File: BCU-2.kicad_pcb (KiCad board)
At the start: 2 copper layers, 106 x 91.4 mm, 92 parts, among them J1 Screw_Terminal_01x04, J2 Conn_01x12_Male, J3 Screw_Terminal_01x04, J4 Conn_01x05_Male, J5 Conn_01x05_Male, J6 Conn_01x04_Male, J7 Conn_01x04_Male, Q1 2N7002, Q2 NTF6P02, Q3 2N7002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

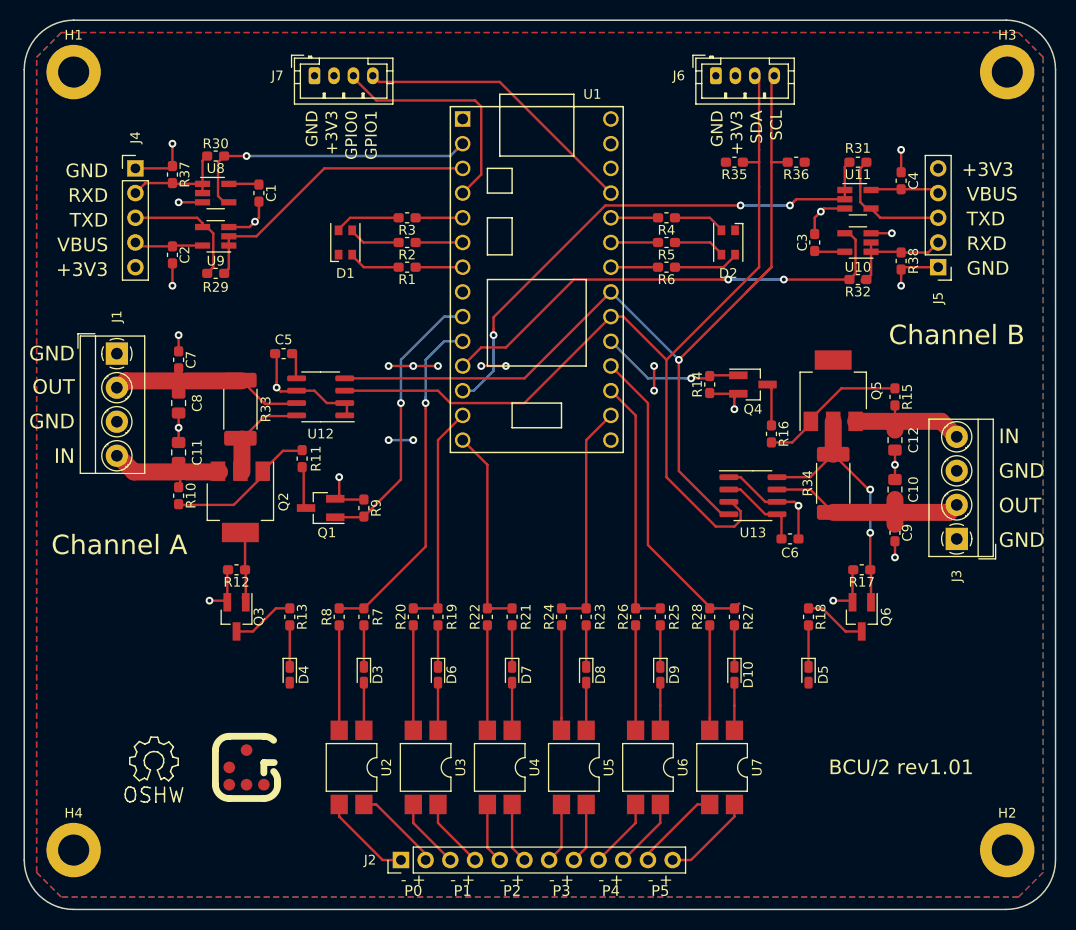
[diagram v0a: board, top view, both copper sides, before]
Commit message: PCB: Remove unneeded stubs to fix track has unconnected end warnings
Signed-off-by: Geert Uytterhoeven <geert@linux-m68k.org>
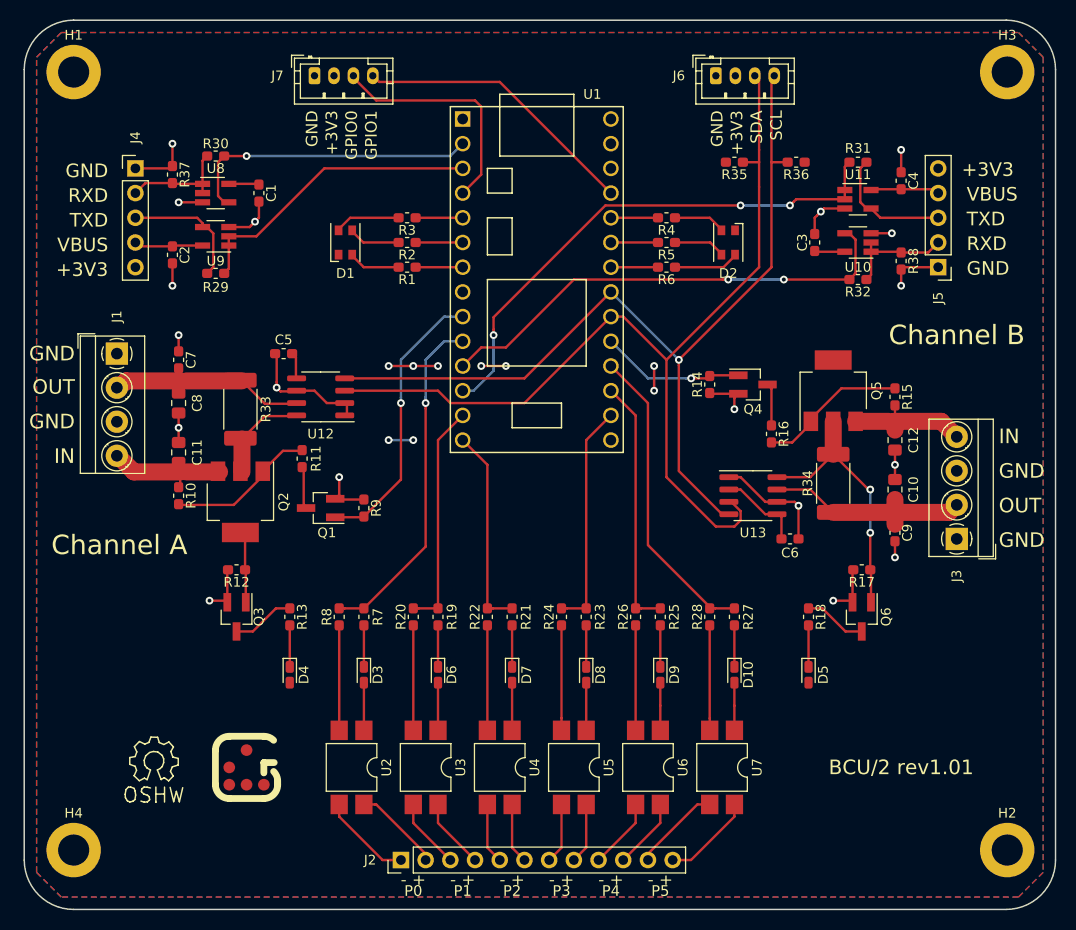
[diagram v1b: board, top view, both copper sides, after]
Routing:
- net SCL: track 97.4 -> 93.4 mm
- net UARTA_RX: track 31.7 -> 30.8 mm
- net P5: track 32.4 -> 31.7 mm
- net GND: track 96.8 -> 96.2 mm
- net LEDA_G: track 5.39 -> 4.84 mm
- net LEDA_B: track 5.39 -> 4.84 mm
- net LEDA_R: track 5.39 -> 4.84 mm
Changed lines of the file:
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@@
   (segment (start 179.475 80.96) (end 176.605 80.96) (width 0.25) (layer "F.Cu") (net 3))
   (segment (start 182.245 92.075) (end 179.705 89.535) (width 0.25) (layer "F.Cu") (net 3))
-  (segment (start 178.75 89.535) (end 178.275 89.535) (width 0.25) (layer "F.Cu") (net 3))
   (segment (start 137.16 81.915) (end 138.2 81.915) (width 0.25) (layer "F.Cu") (net 3))
   (segment (start 193.12 64.455) (end 195.25996 64.455) (width 0.25) (layer "F.Cu") (net 3))
@@
   (segment (start 153.035 78.105) (end 155.575 78.105) (width 0.25) (layer "F.Cu") (net 3))
   (segment (start 200.025 67.945) (end 196.455 67.945) (width 0.25) (layer "F.Cu") (net 3))
-  (segment (start 126.76 101.93) (end 126.685 102.005) (width 0.25) (layer "F.Cu") (net 3))
   (segment (start 126.925 102.4) (end 126.925 99.135) (width 0.25) (layer "F.Cu") (net 3))
   (segment (start 195.58 89.78) (end 195.58 88.265) (width 0.25) (layer "F.Cu") (net 3))
@@
   (segment (start 147.32 128.905) (end 147.32 128.27) (width 0.25) (layer "F.Cu") (net 16))
   (segment (start 142.24 123.19) (end 142.11 123.19) (width 0.25) (layer "F.Cu") (net 16))
-  (segment (start 140.97 123.3) (end 140.97 123.19) (width 0.25) (layer "F.Cu") (net 16))
   (segment (start 142.11 123.19) (end 140.97 123.19) (width 0.25) (layer "F.Cu") (net 16))
   (segment (start 146.05 125.095) (end 149.86 128.905) (width 0.25) (layer "F.Cu") (net 17))
   (segment (start 146.05 123.19) (end 146.05 125.095) (width 0.25) (layer "F.Cu") (net 17))
-  (segment (start 148.59 123.19) (end 148.59 123.3) (width 0.25) (layer "F.Cu") (net 18))
   (segment (start 148.59 123.19) (end 148.59 125.095) (width 0.25) (layer "F.Cu") (net 18))
   (segment (start 148.59 125.095) (end 152.4 128.905) (width 0.25) (layer "F.Cu") (net 18))
@@
   (segment (start 163.83 127.635) (end 162.56 128.905) (width 0.25) (layer "F.Cu") (net 22))
   (segment (start 168.91 123.19) (end 168.91 125.095) (width 0.25) (layer "F.Cu") (net 23))
-  (segment (start 168.91 123.19) (end 168.91 123.3) (width 0.25) (layer "F.Cu") (net 23))
   (segment (start 168.91 125.095) (end 165.1 128.905) (width 0.25) (layer "F.Cu") (net 23))
   (segment (start 171.45 125.095) (end 167.64 128.905) (width 0.25) (layer "F.Cu") (net 24))
@@
   (segment (start 186.93 84.045) (end 186.93 83.795) (width 0.25) (layer "F.Cu") (net 30))
   (segment (start 195.58 80.405) (end 190.07 80.405) (width 0.25) (layer "F.Cu") (net 30))
-  (segment (start 151.13 67.391109) (end 151.13 67.945) (width 0.25) (layer "F.Cu") (net 31))
   (segment (start 151.13 67.945) (end 146.29 67.945) (width 0.25) (layer "F.Cu") (net 31))
   (segment (start 138.365 64.055) (end 138.365 64.155) (width 0.25) (layer "F.Cu") (net 32))
-  (segment (start 144.5 62.905) (end 144.54 62.865) (width 0.25) (layer "F.Cu") (net 32))
   (segment (start 139.555 62.865) (end 138.365 64.055) (width 0.25) (layer "F.Cu") (net 32))
   (segment (start 144.54 62.865) (end 139.555 62.865) (width 0.25) (layer "F.Cu") (net 32))
-  (segment (start 151.13 64.851109) (end 151.13 65.405) (width 0.25) (layer "F.Cu") (net 33))
   (segment (start 151.13 65.405) (end 146.29 65.405) (width 0.25) (layer "F.Cu") (net 33))
-  (segment (start 151.13 62.311109) (end 151.13 62.865) (width 0.25) (layer "F.Cu") (net 34))
   (segment (start 146.29 62.865) (end 151.13 62.865) (width 0.25) (layer "F.Cu") (net 34))
   (segment (start 144.54 65.405) (end 140.915 65.405) (width 0.25) (layer "F.Cu") (net 35))
@@
   (segment (start 176.53 102.87) (end 170.18 96.52) (width 0.25) (layer "F.Cu") (net 49))
   (segment (start 170.18 96.52) (end 170.18 81.915) (width 0.25) (layer "F.Cu") (net 49))
-  (segment (start 179.569072 102.525928) (end 179.07 103.025) (width 0.25) (layer "F.Cu") (net 49))
   (segment (start 170.18 81.915) (end 166.37 78.105) (width 0.25) (layer "F.Cu") (net 49))
   (segment (start 177.105 103.025) (end 179.07 103.025) (width 0.25) (layer "F.Cu") (net 49))
@@
   (segment (start 127.08 61.275) (end 126.625 61.275) (width 0.25) (layer "F.Cu") (net 52))
   (segment (start 126.625 61.275) (end 125.974999 60.624999) (width 0.25) (layer "F.Cu") (net 52))
-  (segment (start 151.13 55.245) (end 150.495 55.88) (width 0.25) (layer "F.Cu") (net 52))
   (segment (start 126.605 56.515) (end 128.905 56.515) (width 0.25) (layer "F.Cu") (net 52))
   (via (at 128.905 56.515) (size 0.8) (drill 0.4) (layers "F.Cu" "B.Cu") (net 52))
@@
   (segment (start 184.15 69.215) (end 178.435 69.215) (width 0.25) (layer "B.Cu") (net 54))
   (segment (start 117.715 65.645) (end 117.475 65.405) (width 0.25) (layer "F.Cu") (net 55))
-  (segment (start 121.36 65.72) (end 121.285 65.645) (width 0.25) (layer "F.Cu") (net 55))
   (segment (start 117.87 65.8) (end 117.475 65.405) (width 0.25) (layer "F.Cu") (net 55))
-  (segment (start 121.365 65.72) (end 121.285 65.8) (width 0.25) (layer "F.Cu") (net 55))
   (segment (start 124.38 65.72) (end 121.365 65.72) (width 0.25) (layer "F.Cu") (net 55))
   (segment (start 121.285 65.8) (end 117.87 65.8) (width 0.25) (layer "F.Cu") (net 55))
-  (segment (start 196.14 60.01) (end 196.215 60.085) (width 0.25) (layer "F.Cu") (net 56))
   (segment (start 199.785 60.085) (end 200.025 60.325) (width 0.25) (layer "F.Cu") (net 56))
-  (segment (start 196.135 60.01) (end 196.215 59.93) (width 0.25) (layer "F.Cu") (net 56))
   (segment (start 196.215 59.93) (end 193.2 59.93) (width 0.25) (layer "F.Cu") (net 56))
   (segment (start 193.2 59.93) (end 193.12 60.01) (width 0.25) (layer "F.Cu") (net 56))
@@
   (segment (start 195.58 93.1575) (end 195.58 91.83) (width 1.75) (layer "F.Cu") (net 62))
   (segment (start 184.545 57.15) (end 182.88 57.15) (width 0.25) (layer "F.Cu") (net 63))
-  (segment (start 180.34 70.485) (end 180.34 70.485032) (width 0.25) (layer "F.Cu") (net 63))
   (segment (start 182.88 48.545) (end 182.88 67.945) (width 0.25) (layer "F.Cu") (net 63))
-  (segment (start 182.88 67.945) (end 180.34 70.485) (width 0.25) (layer "F.Cu") (net 63))
   (segment (start 157.48 79.375) (end 139.225 79.375) (width 0.25) (layer "F.Cu") (net 63))
   (segment (start 183.165 48.26) (end 182.88 48.545) (width 0.25) (layer "F.Cu") (net 63))
-  (segment (start 178.275 93.345) (end 177.8 93.345) (width 0.25) (layer "F.Cu") (net 63))
   (segment (start 173.355 88.9) (end 173.355 78.035675) (width 0.25) (layer "F.Cu") (net 63))
   (segment (start 166.37 70.485) (end 157.48 79.375) (width 0.25) (layer "F.Cu") (net 63))
@@
   (segment (start 181.61 55.88) (end 181.61 48.705) (width 0.25) (layer "F.Cu") (net 64))
   (segment (start 157.48 81.915) (end 149.86 81.915) (width 0.25) (layer "F.Cu") (net 64))
-  (segment (start 178.75 92.075) (end 178.275 92.075) (width 0.25) (layer "F.Cu") (net 64))
   (segment (start 181.61 48.705) (end 181.165 48.26) (width 0.25) (layer "F.Cu") (net 64))
   (segment (start 181.61 59.69) (end 181.61 55.88) (width 0.25) (layer "F.Cu") (net 64))
@@
   (segment (start 133.986298 83.2568) (end 130.783798 83.2568) (width 0.25) (layer "F.Cu") (net 65))
   (segment (start 128.75 95.705) (end 128.27 95.225) (width 0.25) (layer "F.Cu") (net 65))
-  (segment (start 128.51 101.93) (end 128.585 102.005) (width 0.25) (layer "F.Cu") (net 65))
   (segment (start 128.825 99.135) (end 128.75 99.06) (width 0.25) (layer "F.Cu") (net 65))
   (segment (start 128.75 99.06) (end 128.75 95.705) (width 0.25) (layer "F.Cu") (net 65))
@@
   (segment (start 193.04 95.25) (end 193.04 90.805) (width 0.25) (layer "B.Cu") (net 66))
   (segment (start 124.38 56.99) (end 124.855 56.515) (width 0.25) (layer "F.Cu") (net 67))
-  (segment (start 124.46 59.295) (end 124.38 59.375) (width 0.25) (layer "F.Cu") (net 67))
   (segment (start 124.38 59.375) (end 124.38 60.325) (width 0.25) (layer "F.Cu") (net 67))
   (segment (start 124.38 59.375) (end 124.38 56.99) (width 0.25) (layer "F.Cu") (net 67))
@@
   (segment (start 196.135 66.355) (end 196.215 66.435) (width 0.25) (layer "F.Cu") (net 70))
   (segment (start 193.12 66.355) (end 196.135 66.355) (width 0.25) (layer "F.Cu") (net 70))
-  (segment (start 192.165 69.455) (end 192.165 69.215) (width 0.25) (layer "F.Cu") (net 70))
   (segment (start 193.12 66.355) (end 193.12 68.74) (width 0.25) (layer "F.Cu") (net 70))
   (segment (start 193.12 65.405) (end 193.12 66.355) (width 0.25) (layer "F.Cu") (net 70))

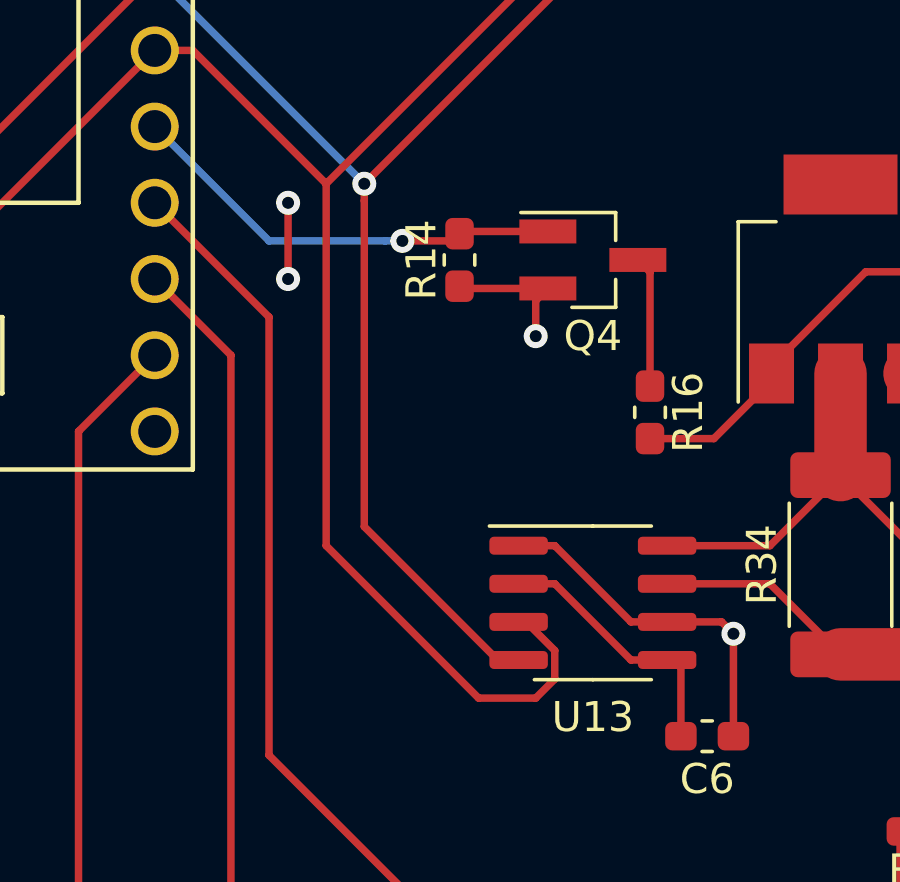
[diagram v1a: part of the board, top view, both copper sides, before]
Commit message: PCB: Fix clearance violation errors
The pads on the INA219xID footprint became slightly larger in KiCad 6.
Move a track, and refill the GND zone.

Signed-off-by: Geert Uytterhoeven <geert@linux-m68k.org>
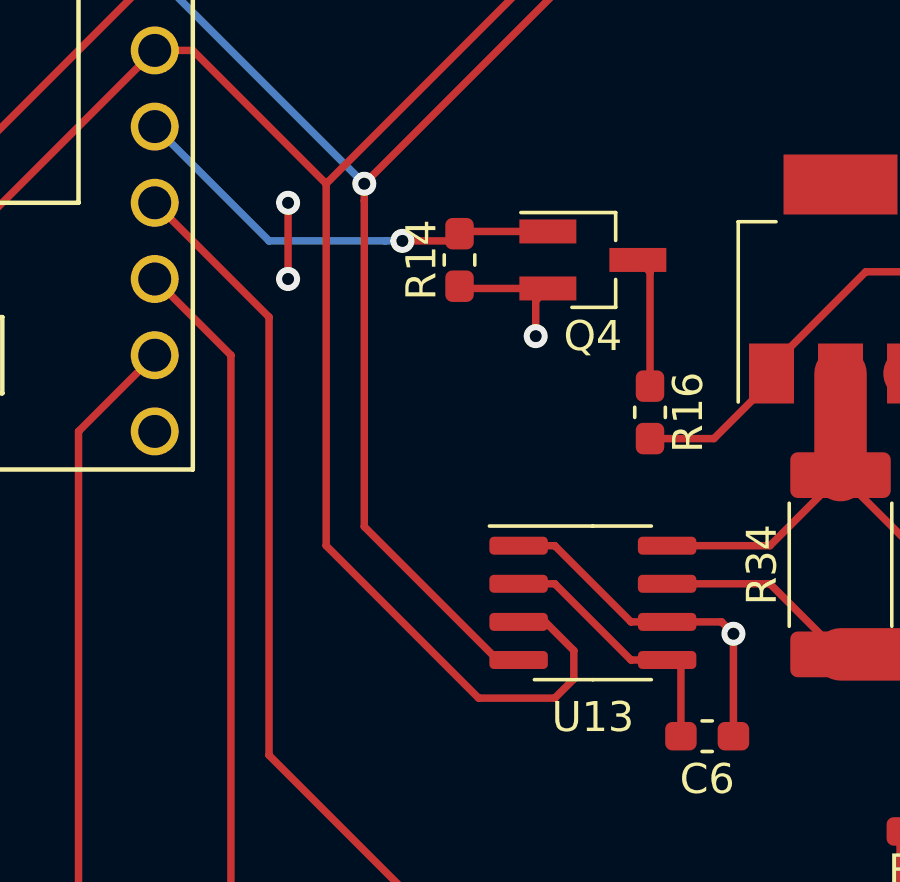
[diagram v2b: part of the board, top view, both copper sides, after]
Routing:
- net SDA: track 98.3 -> 99.8 mm
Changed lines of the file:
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@@
   (segment (start 166.37 70.485) (end 173.35499 77.46999) (width 0.25) (layer "B.Cu") (net 63))
   (segment (start 173.35499 77.46999) (end 173.355 77.46999) (width 0.25) (layer "B.Cu") (net 63))
-  (segment (start 177.165 94.615) (end 179.07 94.615) (width 0.25) (layer "F.Cu") (net 64))
+  (segment (start 177.165 94.615) (end 179.705 94.615) (width 0.25) (layer "F.Cu") (net 64))
+  (segment (start 179.705 94.615) (end 180.34 93.98) (width 0.25) (layer "F.Cu") (net 64))
   (segment (start 172.085 77.47) (end 167.64 73.025) (width 0.25) (layer "F.Cu") (net 64))
-  (segment (start 172.085 89.535) (end 172.085 77.47) (width 0.25) (layer "F.Cu") (net 64))
+  (segment (start 179.385 92.075) (end 178.5 92.075) (width 0.25) (layer "F.Cu") (net 64))
   (segment (start 149.86 81.915) (end 148.59 80.645) (width 0.25) (layer "F.Cu") (net 64))
   (segment (start 166.37 73.025) (end 157.48 81.915) (width 0.25) (layer "F.Cu") (net 64))
-  (segment (start 179.705 93.98) (end 179.705 93.03) (width 0.25) (layer "F.Cu") (net 64))
+  (segment (start 172.085 89.535) (end 177.165 94.615) (width 0.25) (layer "F.Cu") (net 64))
   (segment (start 181.61 55.88) (end 181.61 48.705) (width 0.25) (layer "F.Cu") (net 64))
   (segment (start 157.48 81.915) (end 149.86 81.915) (width 0.25) (layer "F.Cu") (net 64))
   (segment (start 181.61 48.705) (end 181.165 48.26) (width 0.25) (layer "F.Cu") (net 64))
+  (segment (start 180.34 93.98) (end 180.34 93.03) (width 0.25) (layer "F.Cu") (net 64))
   (segment (start 181.61 59.69) (end 181.61 55.88) (width 0.25) (layer "F.Cu") (net 64))
   (segment (start 148.59 80.645) (end 139.225 80.645) (width 0.25) (layer "F.Cu") (net 64))
   (segment (start 172.085 77.47) (end 181.61 67.945) (width 0.25) (layer "F.Cu") (net 64))
-  (segment (start 172.085 89.535) (end 177.165 94.615) (width 0.25) (layer "F.Cu") (net 64))
   (segment (start 181.61 67.945) (end 181.61 59.69) (width 0.25) (layer "F.Cu") (net 64))
-  (segment (start 179.705 93.03) (end 178.75 92.075) (width 0.25) (layer "F.Cu") (net 64))
+  (segment (start 180.34 93.03) (end 179.385 92.075) (width 0.25) (layer "F.Cu") (net 64))
   (segment (start 179.945 57.15) (end 181.61 57.15) (width 0.25) (layer "F.Cu") (net 64))
-  (segment (start 179.07 94.615) (end 179.705 93.98) (width 0.25) (layer "F.Cu") (net 64))
   (segment (start 167.64 73.025) (end 166.37 73.025) (width 0.25) (layer "F.Cu") (net 64))
+  (segment (start 172.085 77.47) (end 172.085 89.535) (width 0.25) (layer "F.Cu") (net 64))
   (segment (start 130.783798 83.2568) (end 128.431298 85.6093) (width 0.25) (layer "F.Cu") (net 65))
   (segment (start 128.431298 88.9968) (end 128.431298 85.6093) (width 1.75) (layer "F.Cu") (net 65))
@@
   (zone (net 4) (net_name "+3V3") (layer "F.Cu") (hatch edge 0.508)
     (connect_pads (clearance 0.508))
-    (min_thickness 0.254)
+    (min_thickness 0.254) (filled_areas_thickness no)
     (fill yes (thermal_gap 0.508) (thermal_bridge_width 0.508))
     (polygon
@@
   (zone (net 3) (net_name "GND") (layer "B.Cu") (hatch edge 0.508)
     (connect_pads (clearance 0.508))
-    (min_thickness 0.254)
+    (min_thickness 0.254) (filled_areas_thickness no)
     (fill yes (thermal_gap 0.508) (thermal_bridge_width 0.508))
     (polygon
